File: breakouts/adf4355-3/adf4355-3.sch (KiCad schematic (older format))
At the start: 57 parts, among them P1 CONN_01X02, P2 CONN_01X06, P3 CONN_01X05, P4 CONN_01X05, P5 CONN_01X05, U1 ADM7150, U2 TCM-63AX+, U3 TCM-63AX+, U4 ADF4355-3, U5 mounting_box, U6 TXCO

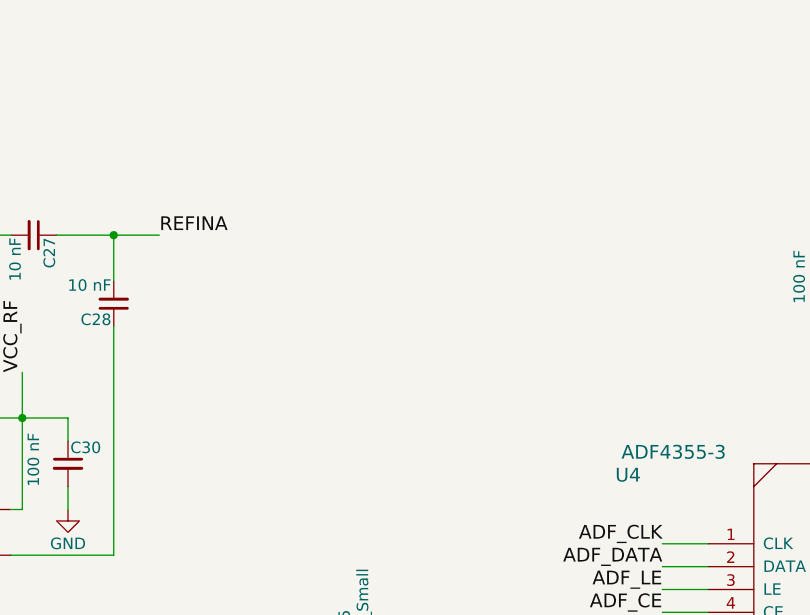
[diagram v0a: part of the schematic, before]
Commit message: ready to order demod, pcm breakout, booster, and synth
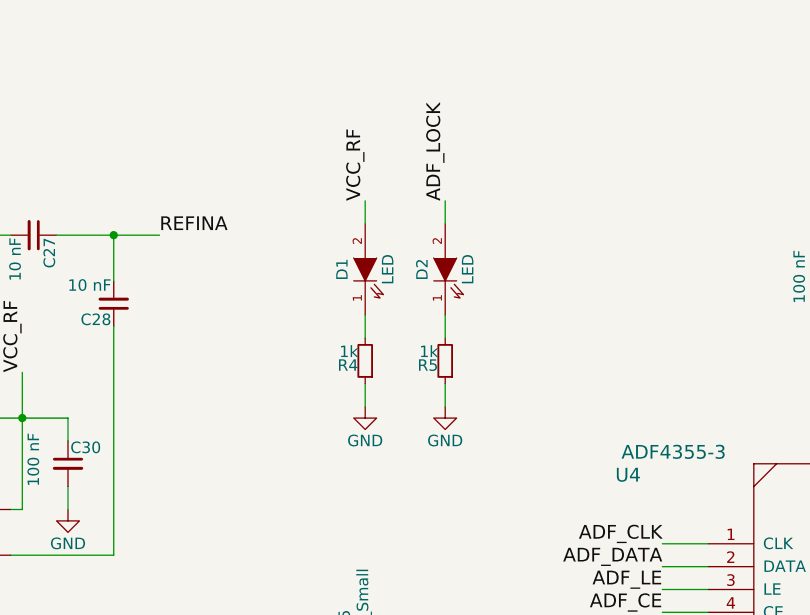
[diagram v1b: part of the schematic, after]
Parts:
- added D1, D2: LED, LEDs:LED_0603, symbol LED
- added R4, R5: 1k, Resistors_SMD:R_0402, symbol R_Small
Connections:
- net ADF_LOCK: now also D2.2 (A)
- net GND: now also R4.1, R5.1
- net VCC_RF: now also D1.2 (A)
- new net: D1.1 (K), R4.2
- new net: D2.1 (K), R5.2
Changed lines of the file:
@@
 	6200 3150 6200 3000
 Connection ~ 6200 3000
+$Comp
+L LED D1
+U 1 1 56DEB37C
+P 5950 1400
+F 0 "D1" H 5950 1500 50  0000 C CNN
+F 1 "LED" H 5950 1300 50  0000 C CNN
+F 2 "LEDs:LED_0603" H 5950 1400 50  0001 C CNN
+F 3 "" H 5950 1400 50  0000 C CNN
+	1    5950 1400
+	0    -1   -1   0
+$EndComp
+$Comp
+L R_Small R4
+U 1 1 56DEBAC8
+P 5950 1800
+F 0 "R4" H 5980 1820 50  0000 L CNN
+F 1 "1k" H 5980 1760 50  0000 L CNN
+F 2 "Resistors_SMD:R_0402" H 5950 1800 50  0001 C CNN
+F 3 "" H 5950 1800 50  0000 C CNN
+	1    5950 1800
+	-1   0    0    1
+$EndComp
+$Comp
+L GND #PWR048
+U 1 1 56DEBF4D
+P 5950 2000
+F 0 "#PWR048" H 5950 1750 50  0001 C CNN
+F 1 "GND" H 5950 1850 50  0000 C CNN
+F 2 "" H 5950 2000 50  0000 C CNN
+F 3 "" H 5950 2000 50  0000 C CNN
+	1    5950 2000
+	1    0    0    -1
+$EndComp
+Wire Wire Line
+	5950 2000 5950 1900
+Wire Wire Line
+	5950 1700 5950 1600
+Wire Wire Line
+	5950 1200 5950 1100
+Text Label 5950 1100 1    60   ~ 0
+VCC_RF
+Text Label 6300 1100 1    60   ~ 0
+ADF_LOCK
+$Comp
+L LED D2
+U 1 1 56DECBF8
+P 6300 1400
+F 0 "D2" H 6300 1500 50  0000 C CNN
+F 1 "LED" H 6300 1300 50  0000 C CNN
+F 2 "LEDs:LED_0603" H 6300 1400 50  0001 C CNN
+F 3 "" H 6300 1400 50  0000 C CNN
+	1    6300 1400
+	0    -1   -1   0
+$EndComp
+$Comp
+L R_Small R5
+U 1 1 56DECD0A
+P 6300 1800
+F 0 "R5" H 6330 1820 50  0000 L CNN
+F 1 "1k" H 6330 1760 50  0000 L CNN
+F 2 "Resistors_SMD:R_0402" H 6300 1800 50  0001 C CNN
+F 3 "" H 6300 1800 50  0000 C CNN
+	1    6300 1800
+	-1   0    0    1
+$EndComp
+$Comp
+L GND #PWR049
+U 1 1 56DECDDB
+P 6300 2000
+F 0 "#PWR049" H 6300 1750 50  0001 C CNN
+F 1 "GND" H 6300 1850 50  0000 C CNN
+F 2 "" H 6300 2000 50  0000 C CNN
+F 3 "" H 6300 2000 50  0000 C CNN
+	1    6300 2000
+	1    0    0    -1
+$EndComp
+Wire Wire Line
+	6300 1900 6300 2000
+Wire Wire Line
+	6300 1600 6300 1700
+Wire Wire Line
+	6300 1100 6300 1200
 $EndSCHEMATC

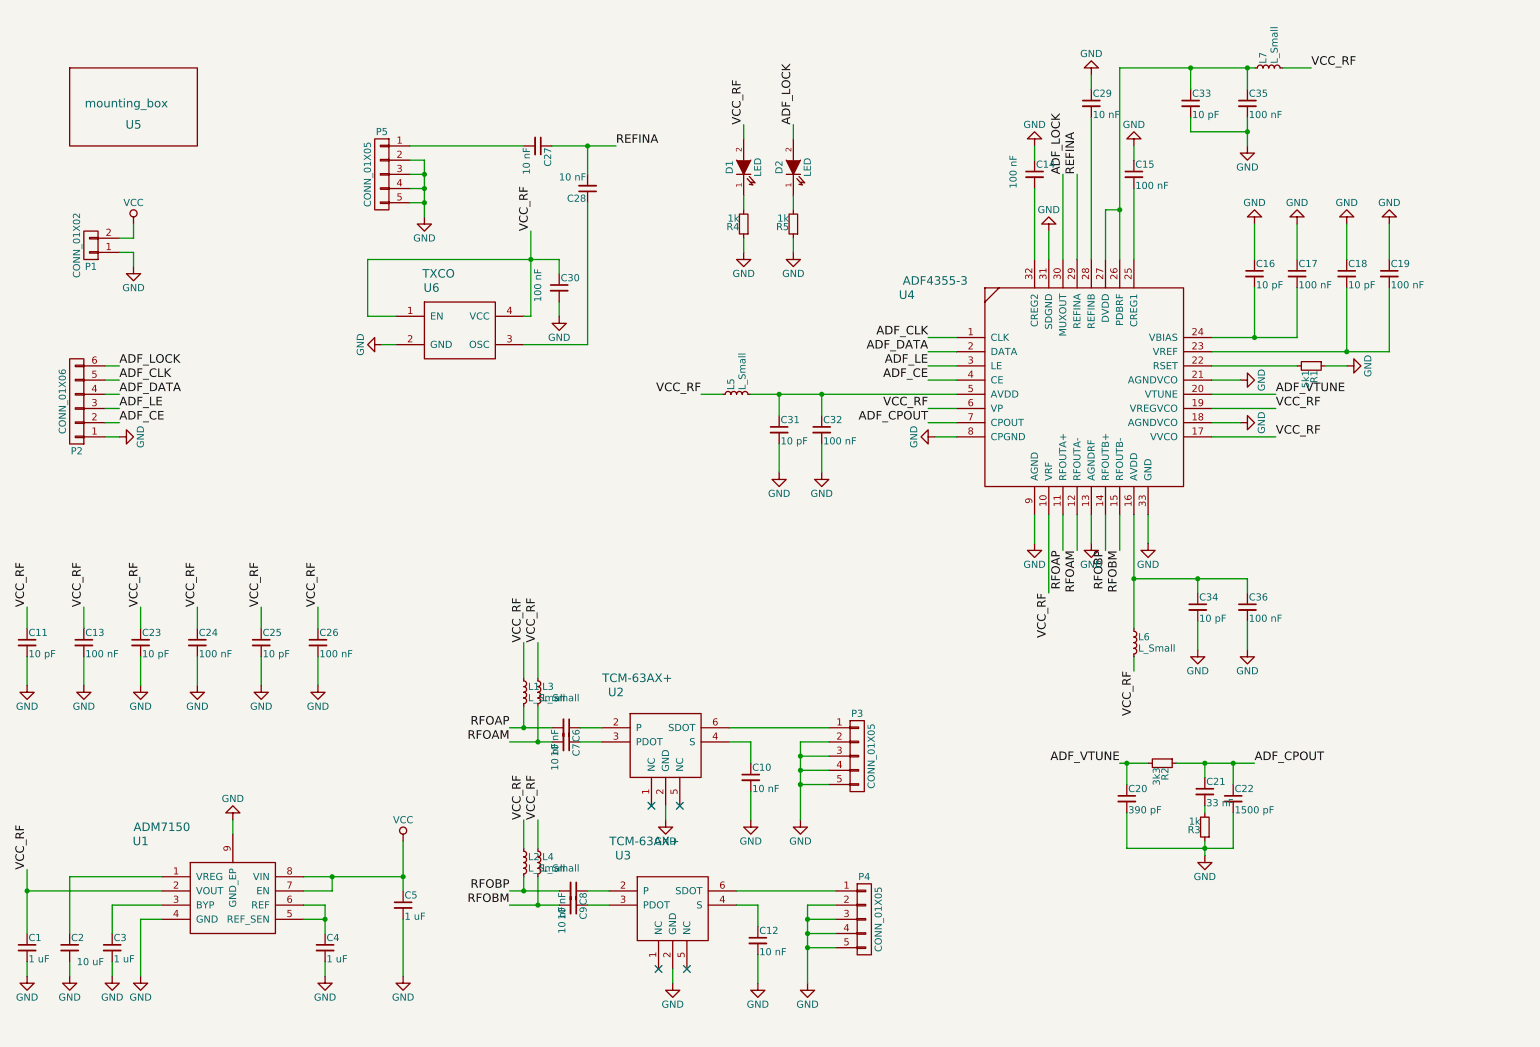
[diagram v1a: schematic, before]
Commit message: started variable attenuator, revised synth, and added power splittert to detect board
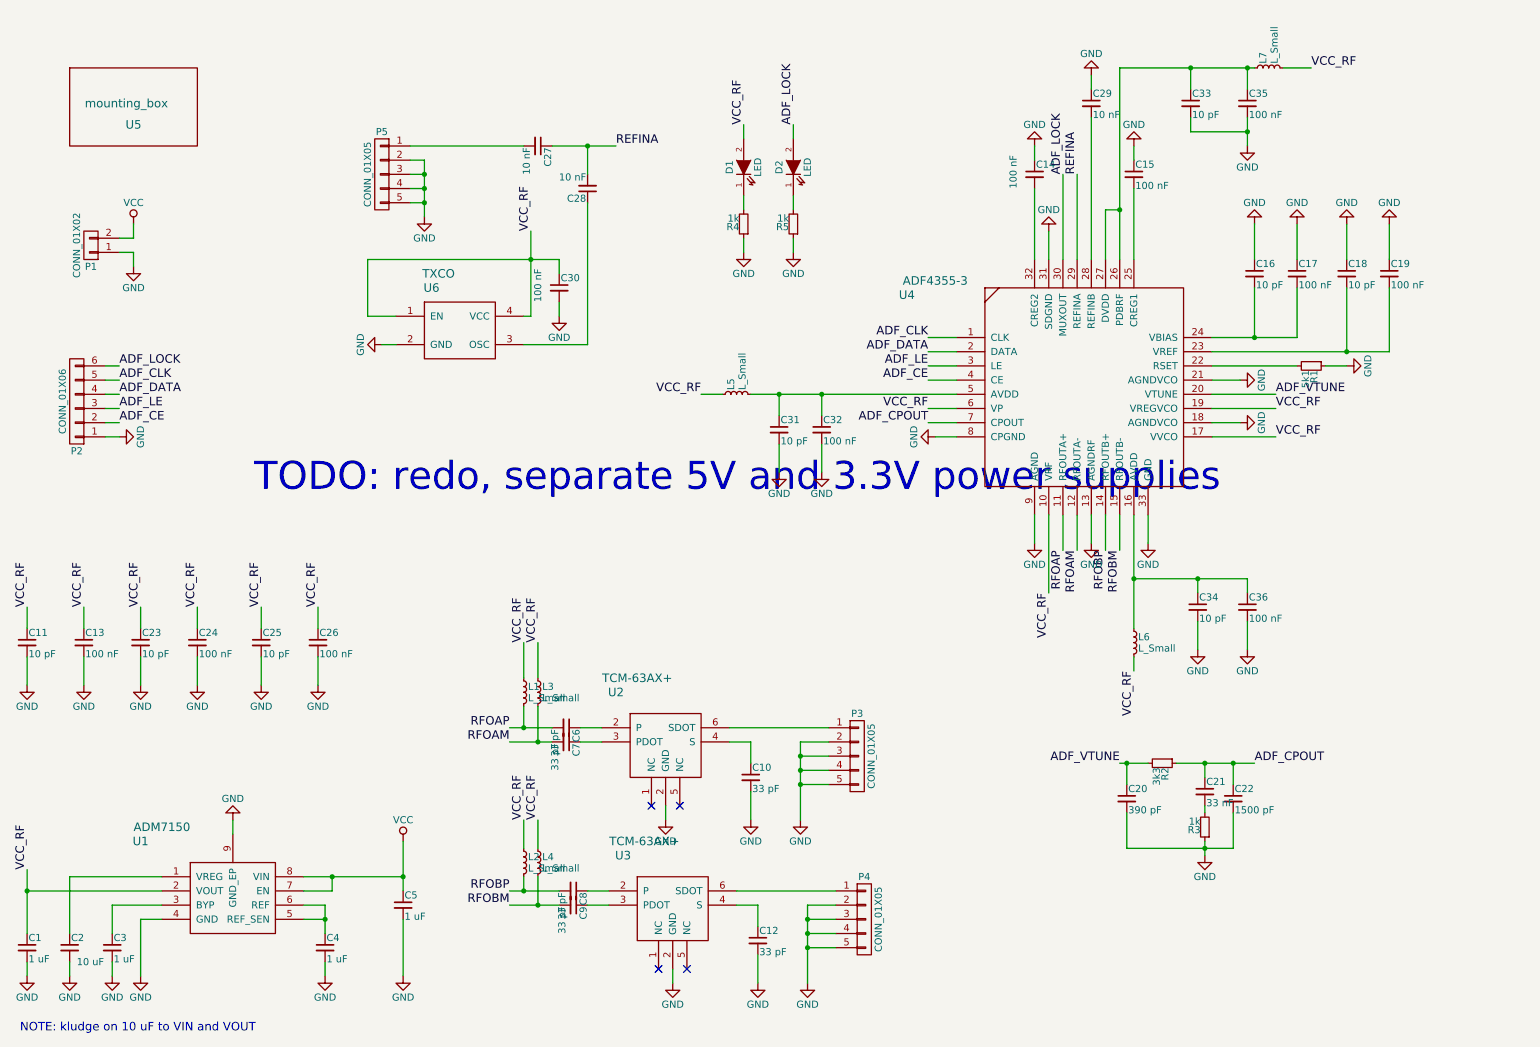
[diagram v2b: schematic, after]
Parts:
- C10, C12, C6, C7, C8, C9: value 10 nF -> 33 pF
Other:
- note added: "NOTE: kludge on 10 uF to VIN and VOUT"
- note added: "TODO: redo, separate 5V and 3.3V power supplies"
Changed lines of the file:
@@
 LIBS:contrib
 LIBS:valves
-LIBS:adf4355-3
-LIBS:adl5380
-LIBS:tcm-63ax+
 LIBS:mounting_box
 LIBS:adm7150
@@
 P 6050 6850
 F 0 "C12" H 6060 6920 50  0000 L CNN
-F 1 "10 nF" H 6060 6770 50  0000 L CNN
+F 1 "33 pF" H 6060 6770 50  0000 L CNN
 F 2 "Capacitors_SMD:C_0402" H 6050 6850 50  0001 C CNN
 F 3 "" H 6050 6850 50  0000 C CNN
@@
 P 6000 5700
 F 0 "C10" H 6010 5770 50  0000 L CNN
-F 1 "10 nF" H 6010 5620 50  0000 L CNN
+F 1 "33 pF" H 6010 5620 50  0000 L CNN
 F 2 "Capacitors_SMD:C_0402" H 6000 5700 50  0001 C CNN
 F 3 "" H 6000 5700 50  0000 C CNN
@@
 P 4750 6500
 F 0 "C8" H 4760 6570 50  0000 L CNN
-F 1 "10 nF" H 4760 6420 50  0000 L CNN
+F 1 "33 pF" H 4760 6420 50  0000 L CNN
 F 2 "Capacitors_SMD:C_0402" H 4750 6500 50  0001 C CNN
 F 3 "" H 4750 6500 50  0000 C CNN
@@
 P 4750 6600
 F 0 "C9" H 4760 6670 50  0000 L CNN
-F 1 "10 nF" H 4760 6520 50  0000 L CNN
+F 1 "33 pF" H 4760 6520 50  0000 L CNN
 F 2 "Capacitors_SMD:C_0402" H 4750 6600 50  0001 C CNN
 F 3 "" H 4750 6600 50  0000 C CNN
@@
 P 4700 5350
 F 0 "C6" H 4710 5420 50  0000 L CNN
-F 1 "10 nF" H 4710 5270 50  0000 L CNN
+F 1 "33 pF" H 4710 5270 50  0000 L CNN
 F 2 "Capacitors_SMD:C_0402" H 4700 5350 50  0001 C CNN
 F 3 "" H 4700 5350 50  0000 C CNN
@@
 P 4700 5450
 F 0 "C7" H 4710 5520 50  0000 L CNN
-F 1 "10 nF" H 4710 5370 50  0000 L CNN
+F 1 "33 pF" H 4710 5370 50  0000 L CNN
 F 2 "Capacitors_SMD:C_0402" H 4700 5450 50  0001 C CNN
 F 3 "" H 4700 5450 50  0000 C CNN
@@
 Wire Wire Line
 	6300 1100 6300 1200
+Text Notes 850  7500 0    60   ~ 0
+NOTE: kludge on 10 uF to VIN and VOUT
+Text Notes 2500 3700 0    197  ~ 0
+TODO: redo, separate 5V and 3.3V power supplies
 $EndSCHEMATC
